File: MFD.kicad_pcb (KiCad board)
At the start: 2 copper layers, 209.6 x 209.6 mm, 43 parts, among them U1 4051, U2 ProMicro

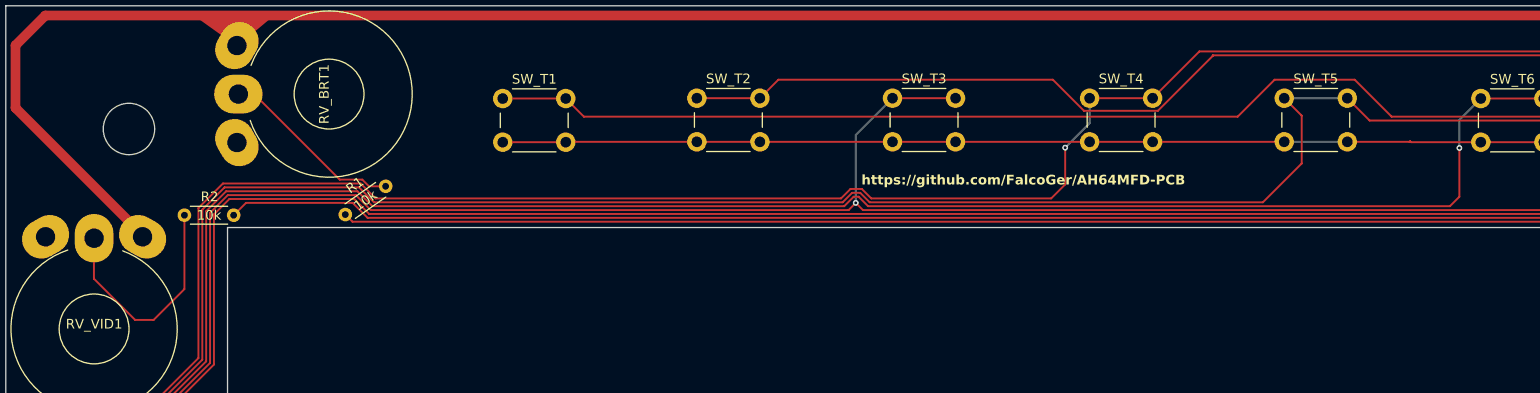
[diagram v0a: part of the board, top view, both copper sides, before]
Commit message: re-adds open hardware silkscreen adds open hardware symbol to schematic adds net names
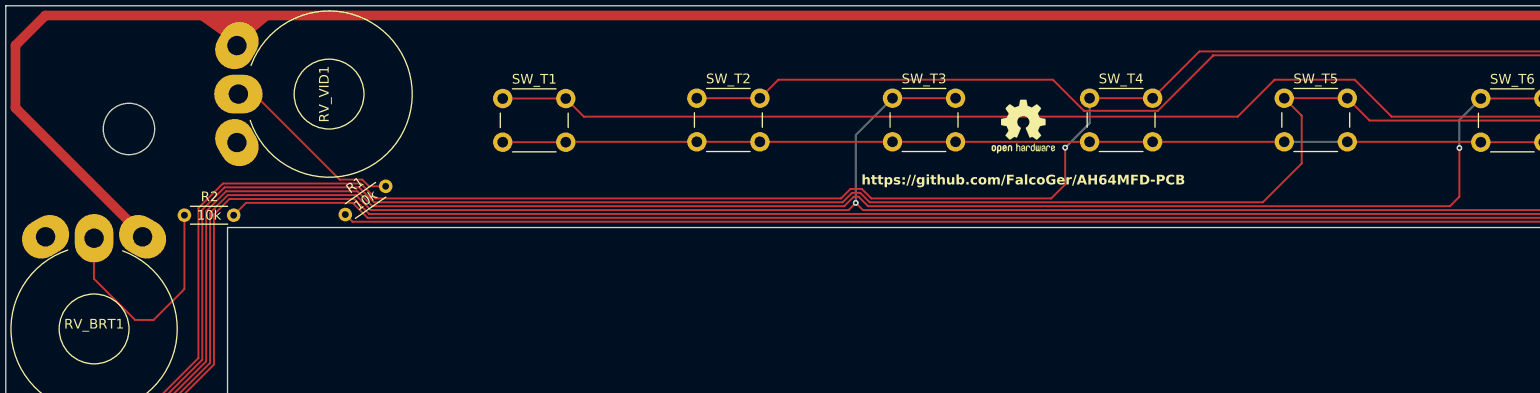
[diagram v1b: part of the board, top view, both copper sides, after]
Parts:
- added SYM1: Logo_Open_Hardware_Small, Symbol:OSHW-Logo2_7.3x6mm_SilkScreen, F.Cu at (163.0, 53.2)
- renumbered RV_VID1 to RV_BRT1, RV_BRT1 to RV_VID1
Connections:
- net Net-(U1-A) renamed /ADDR_0
- net Net-(U1-B) renamed /ADDR_1
- net Net-(U1-C) renamed /ADDR_2
- net Net-(U1-Inh) renamed /MUX_Inhibbit
- net Net-(U1-X) renamed /MUX_Common
- net Net-(U1-X0) renamed /COL_0
- net Net-(U1-X1) renamed /COL_1
- net Net-(U1-X2) renamed /COL_2
- net Net-(U1-X3) renamed /COL_3
- net Net-(U1-X4) renamed /COL_4
- net Net-(U1-X5) renamed /COL_5
- net Net-(U1-X6) renamed /COL_6
- net Net-(U1-X7) renamed /COL_7
- net Net-(U2-A0) renamed /Analog_VID
- net Net-(U2-A1) renamed /Analog_BRT
- net Net-(U2-D4/A6) renamed /ROW_C
- net Net-(U2-D5) renamed /ROW_D
- net Net-(U2-SCL/D3) renamed /ROW_B
- net Net-(U2-SDA/D2) renamed /ROW_A
